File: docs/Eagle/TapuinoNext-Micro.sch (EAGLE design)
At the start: 10 parts

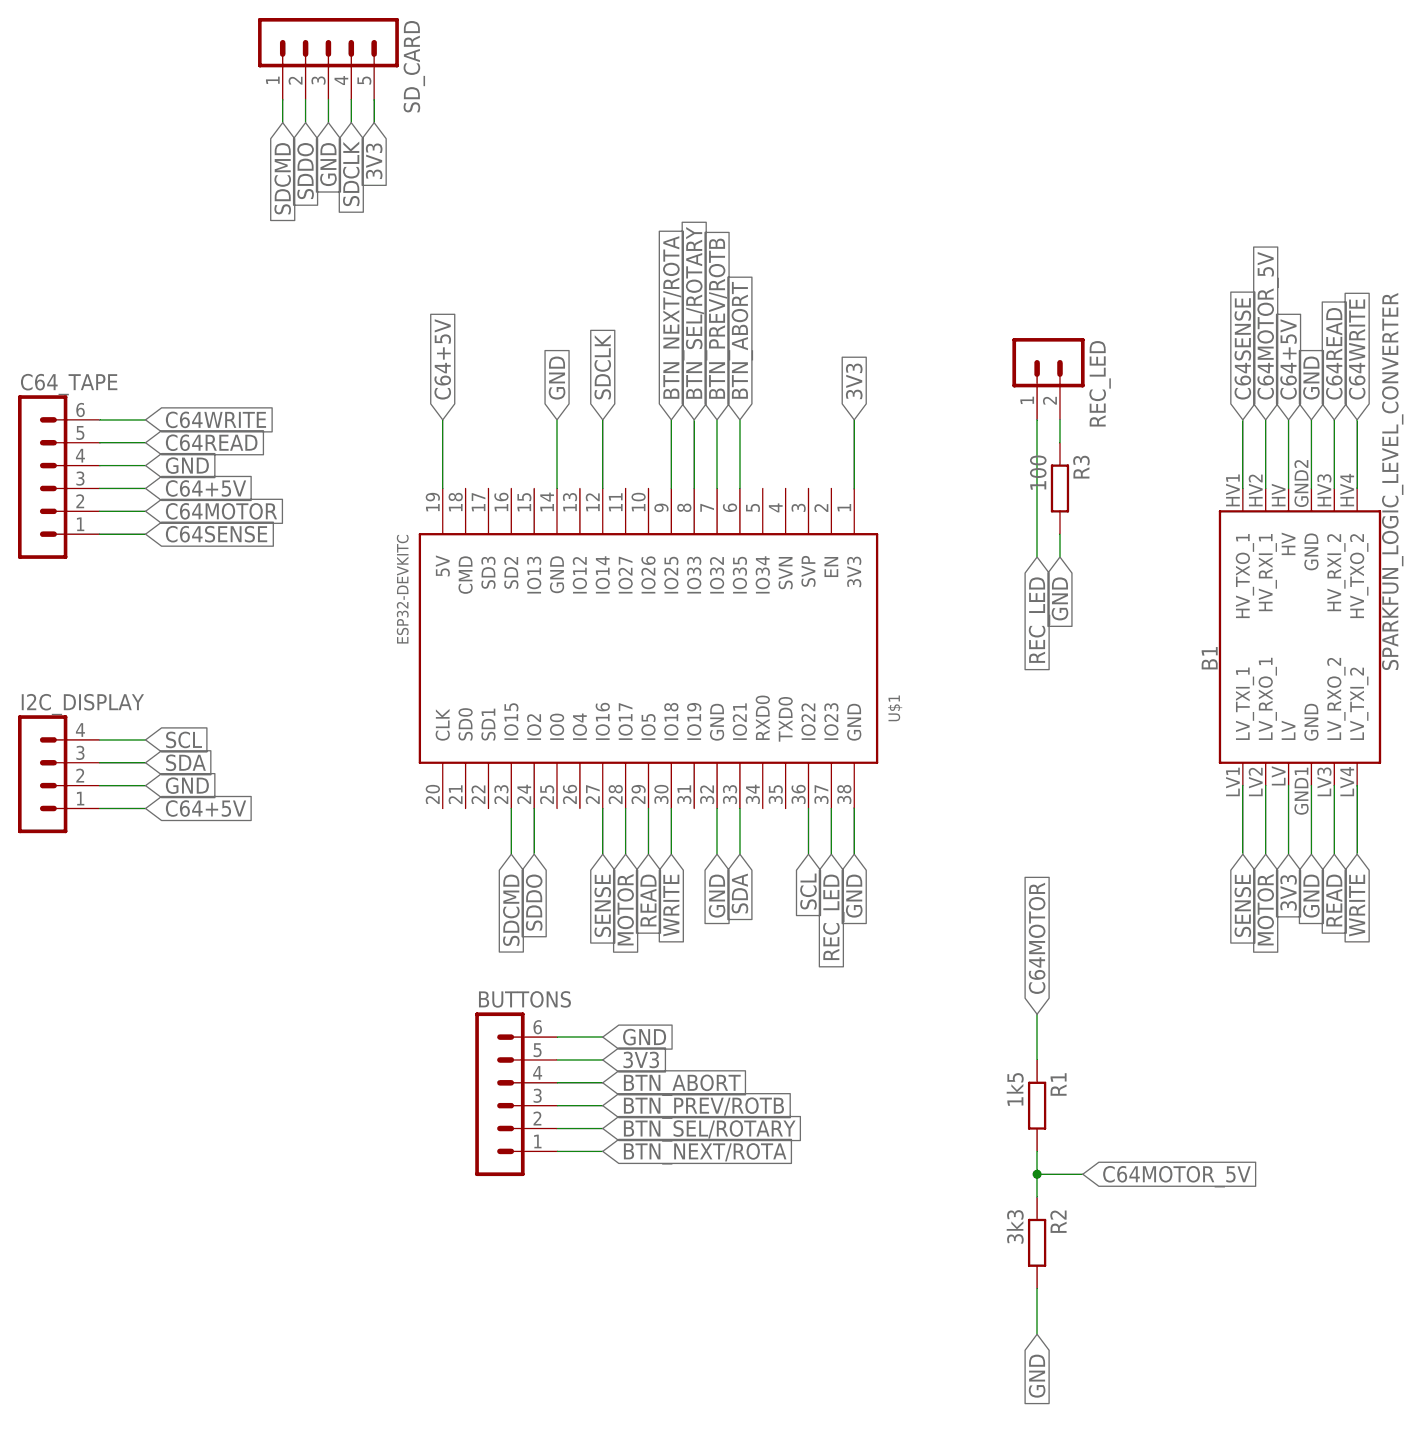
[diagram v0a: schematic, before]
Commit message: fixed definition for OLED1306 added the correct part for tthe ESP32 Devkit added a micro board for system builders (trying to keep this to the smallest footprint possible for custom builds) fixed the foot print on the reference board need to sort out constant changes to config.h to allow users changes outside of source control
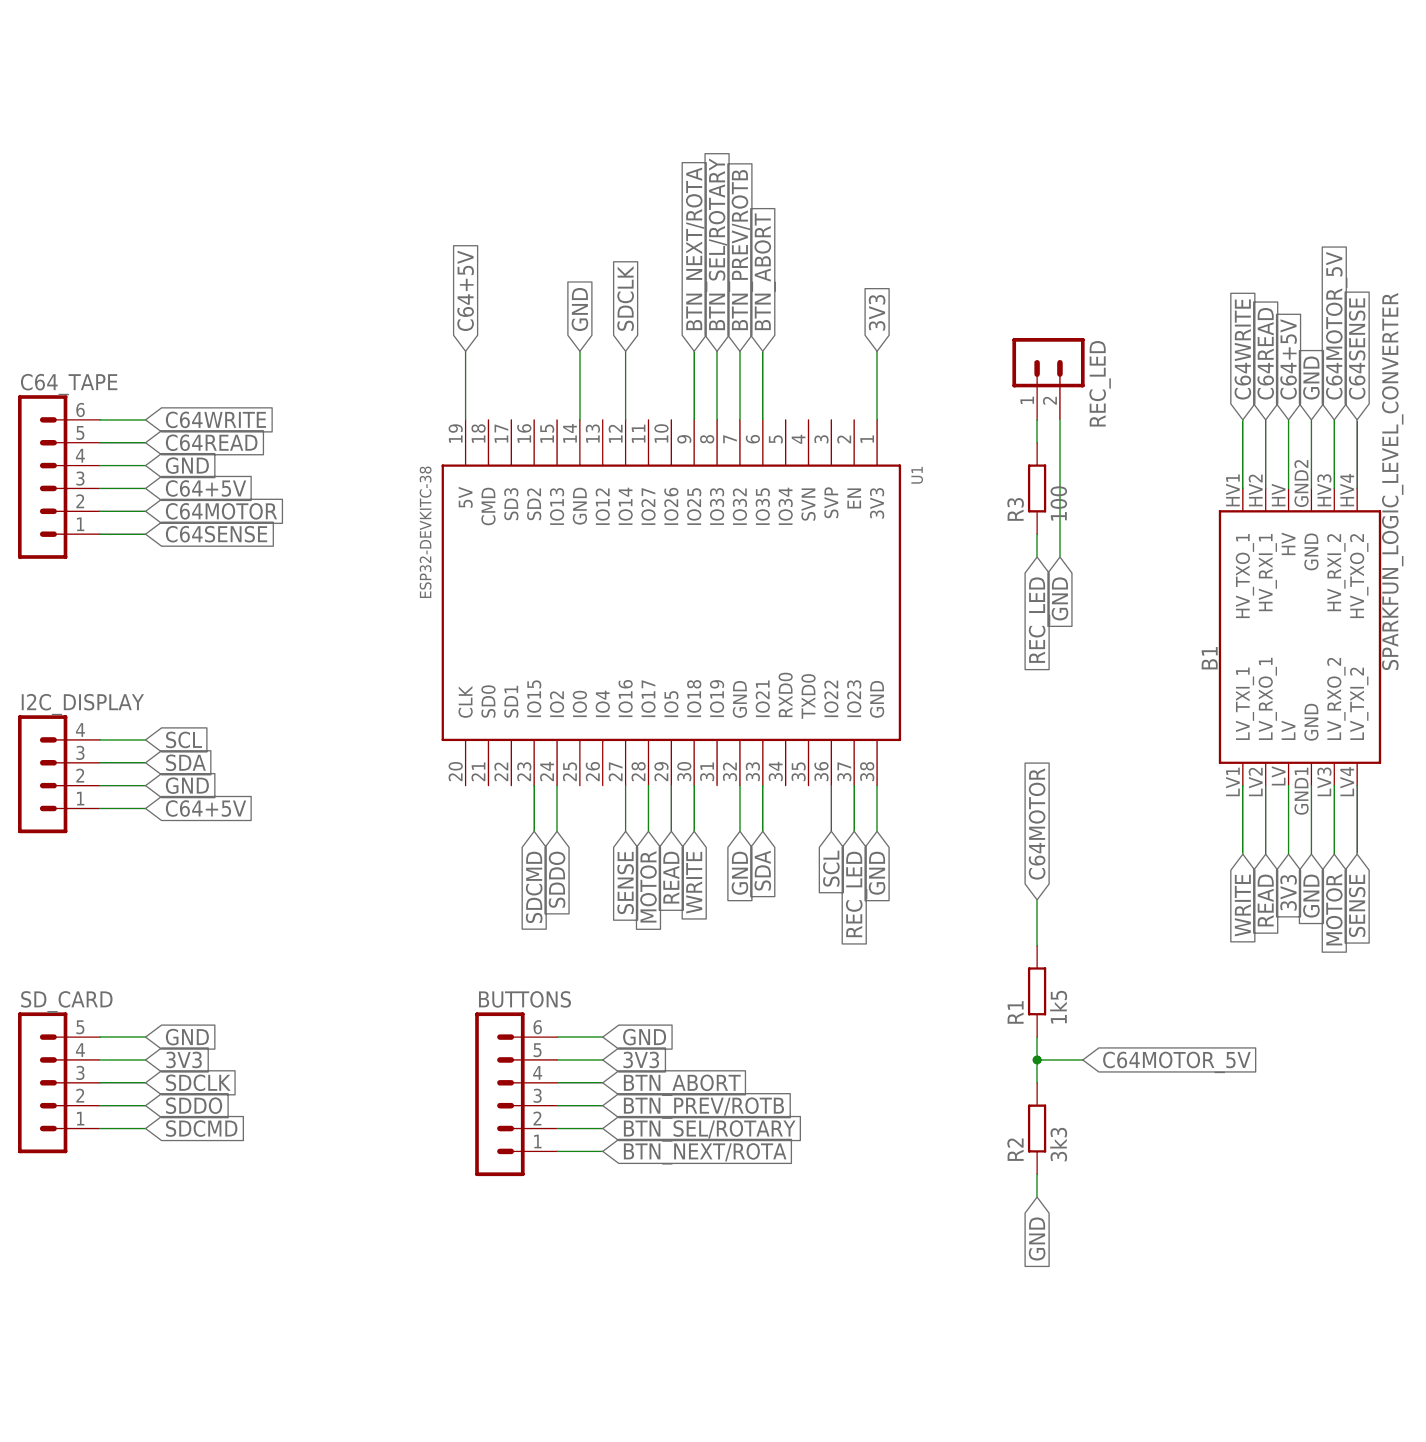
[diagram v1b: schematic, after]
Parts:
- removed U$1: ESP32DEVKITC, ESP32-DEVKITC:ESP32DEVKITC
- added U1: ESP32-DEVKITC-38, ESP32-DEVKITC-38PIN:ESP32-DEVKITC-38
- R1, R2, R3: device rcl:R-EU_0204/7 -> rcl:R-EU_M0805
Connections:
- removed net N$2: R3.1, REC_LED.2
- new net N$1: R3.2, REC_LED.1
- net 3V3: now also SD_CARD.4, U1.3V3; no longer SD_CARD.5, U$1.3V3
- net BTN_ABORT: now also U1.IO35; no longer U$1.IO35
- net BTN_NEXT/ROTA: now also U1.IO25; no longer U$1.IO25
- net BTN_PREV/ROTB: now also U1.IO32; no longer U$1.IO32
- net BTN_SEL/ROTARY: now also U1.IO33; no longer U$1.IO33
- net C64+5V: now also U1.5V; no longer U$1.5V
- net C64MOTOR: now also R1.2; no longer R1.1
- net C64MOTOR_5V: now also B1.HV_RXI_2, R1.1, R2.2; no longer B1.HV_RXI_1, R1.2, R2.1
- net C64READ: now also B1.HV_RXI_1; no longer B1.HV_RXI_2
- net C64SENSE: now also B1.HV_TXO_2; no longer B1.HV_TXO_1
- net C64WRITE: now also B1.HV_TXO_1; no longer B1.HV_TXO_2
- net GND: now also R2.1, REC_LED.2, SD_CARD.5, U1.GND@14, U1.GND@32, U1.GND@38; no longer R2.2, R3.2, SD_CARD.3, U$1.GND@14, U$1.GND@32, U$1.GND@38
- net MOTOR: now also B1.LV_RXO_2, U1.IO17; no longer B1.LV_RXO_1, U$1.IO17
- net READ: now also B1.LV_RXO_1, U1.IO5; no longer B1.LV_RXO_2, U$1.IO5
- net REC_LED: now also R3.1, U1.IO23; no longer REC_LED.1, U$1.IO23
- net SCL: now also U1.IO22; no longer U$1.IO22
- net SDA: now also U1.IO21; no longer U$1.IO21
- net SDCLK: now also SD_CARD.3, U1.IO14; no longer SD_CARD.4, U$1.IO14
- net SDCMD: now also U1.IO15; no longer U$1.IO15
- net SDDO: now also U1.IO2; no longer U$1.IO2
- net SENSE: now also B1.LV_TXI_2, U1.IO16; no longer B1.LV_TXI_1, U$1.IO16
- net WRITE: now also B1.LV_TXI_1, U1.IO18; no longer B1.LV_TXI_2, U$1.IO18
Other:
- moved on the sheet: R1, R2, R3, SD_CARD

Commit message: Changed rotary wiring back to original to match stripboard
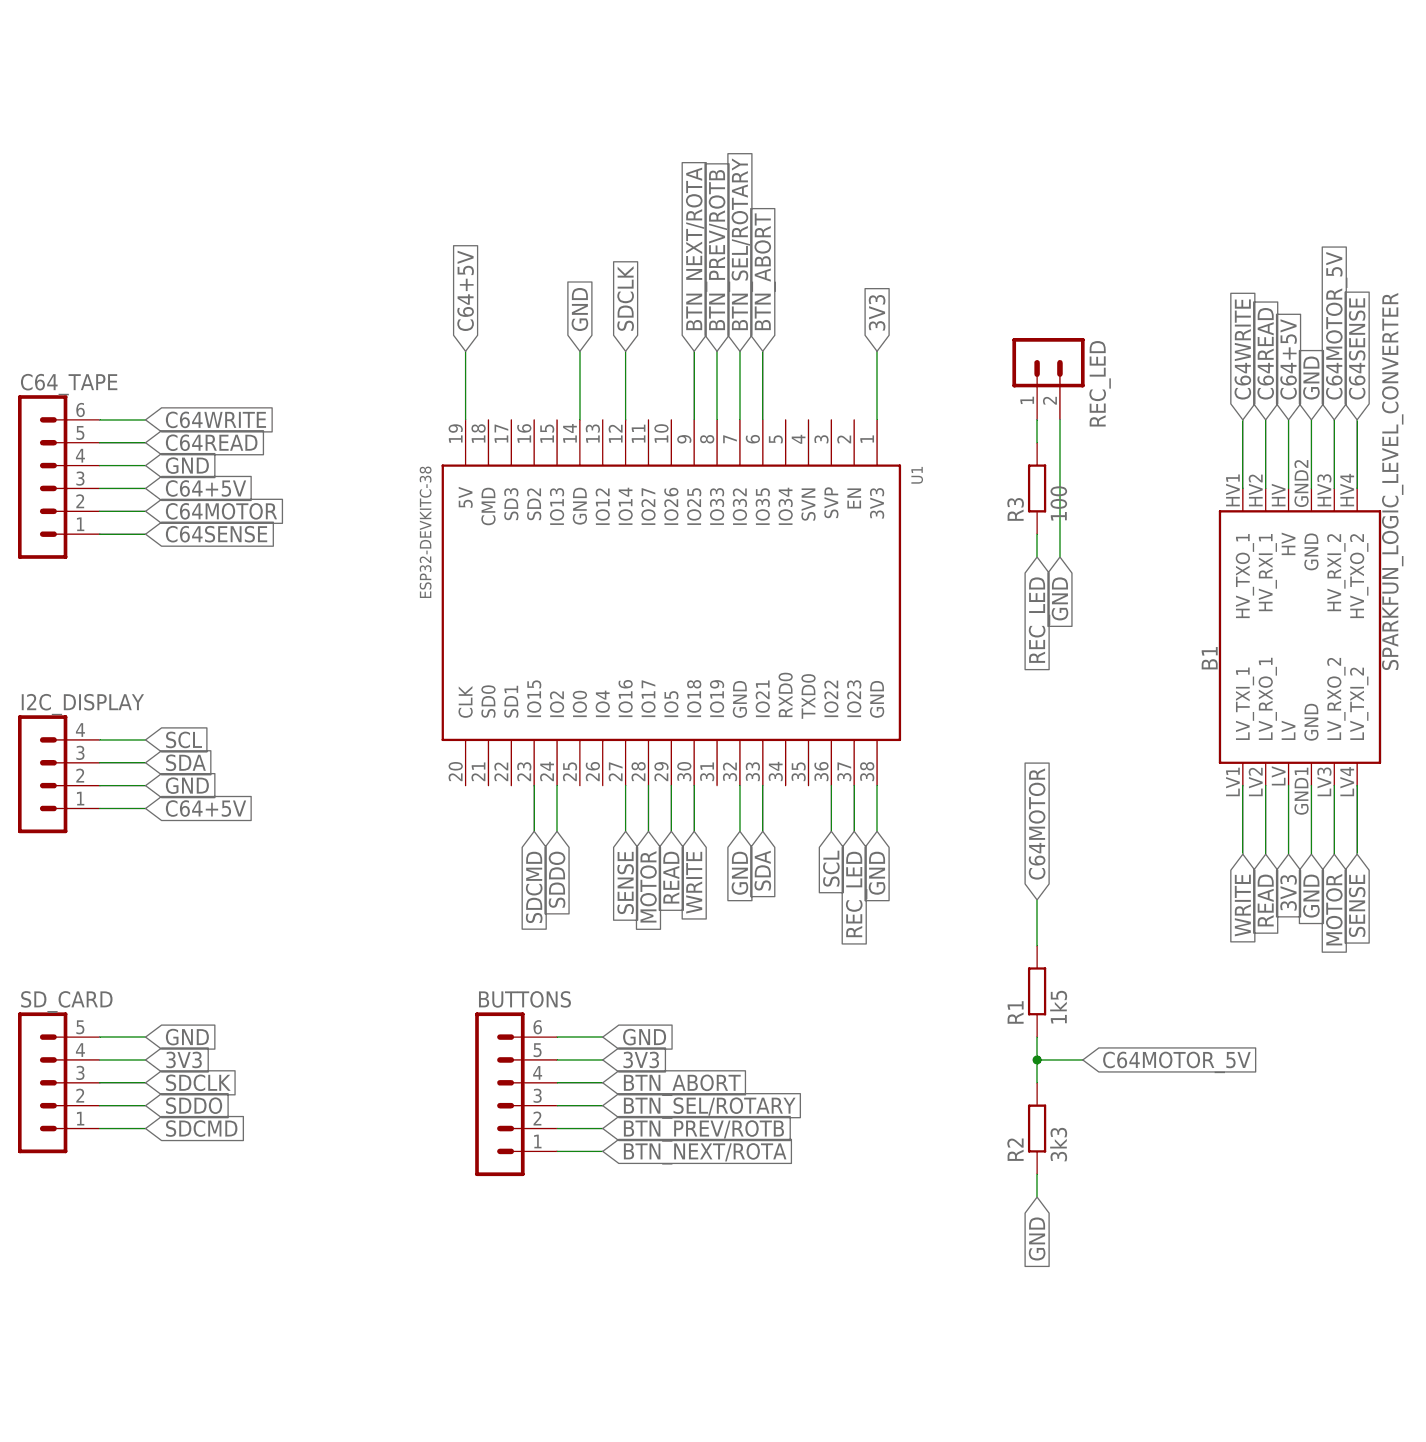
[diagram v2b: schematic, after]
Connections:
- net BTN_PREV/ROTB: now also BUTTONS.2, U1.IO33; no longer BUTTONS.3, U1.IO32
- net BTN_SEL/ROTARY: now also BUTTONS.3, U1.IO32; no longer BUTTONS.2, U1.IO33
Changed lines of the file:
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@@
 <net name="BTN_PREV/ROTB" class="0">
 <segment>
+<pinref part="U1" gate="G$1" pin="IO33"/>
+<wire x1="53.34" y1="68.58" x2="53.34" y2="76.2" width="0.1524" layer="91"/>
+<label x="53.34" y="76.2" size="1.778" layer="95" rot="R90" xref="yes"/>
+</segment>
+<segment>
+<pinref part="BUTTONS" gate="1" pin="2"/>
+<wire x1="35.56" y1="-10.16" x2="40.64" y2="-10.16" width="0.1524" layer="91"/>
+<label x="40.64" y="-10.16" size="1.778" layer="95" xref="yes"/>
+</segment>
+</net>
+<net name="BTN_SEL/ROTARY" class="0">
+<segment>
+<pinref part="U1" gate="G$1" pin="IO32"/>
 <wire x1="55.88" y1="68.58" x2="55.88" y2="76.2" width="0.1524" layer="91"/>
 <label x="55.88" y="76.2" size="1.778" layer="95" rot="R90" xref="yes"/>
-<pinref part="U1" gate="G$1" pin="IO32"/>
 </segment>
 <segment>
@@
 </segment>
 </net>
-<net name="BTN_SEL/ROTARY" class="0">
-<segment>
-<wire x1="53.34" y1="68.58" x2="53.34" y2="76.2" width="0.1524" layer="91"/>
-<label x="53.34" y="76.2" size="1.778" layer="95" rot="R90" xref="yes"/>
-<pinref part="U1" gate="G$1" pin="IO33"/>
-</segment>
-<segment>
-<pinref part="BUTTONS" gate="1" pin="2"/>
-<wire x1="35.56" y1="-10.16" x2="40.64" y2="-10.16" width="0.1524" layer="91"/>
-<label x="40.64" y="-10.16" size="1.778" layer="95" xref="yes"/>
-</segment>
-</net>

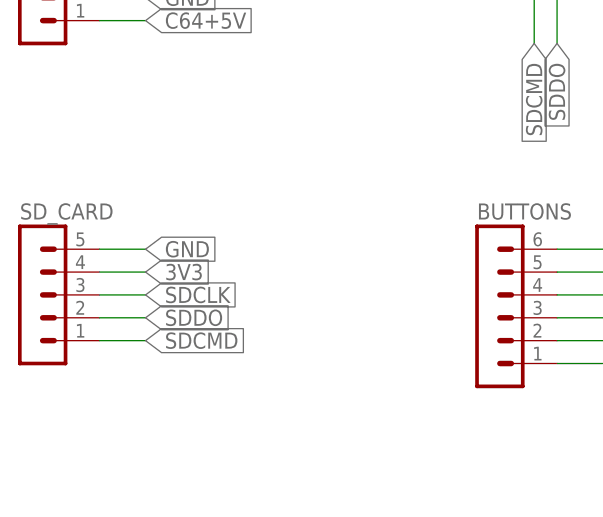
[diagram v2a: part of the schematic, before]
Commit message: Fixed pinout across all of the schematics, hopefully for the last time
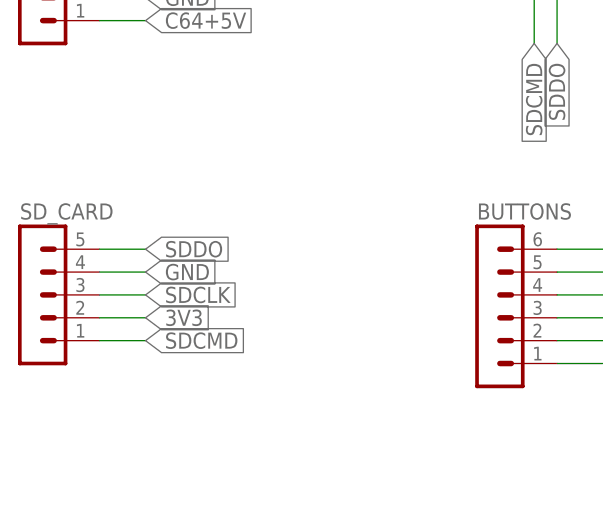
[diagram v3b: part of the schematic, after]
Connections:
- net 3V3: now also SD_CARD.2; no longer SD_CARD.4
- net GND: now also SD_CARD.4; no longer SD_CARD.5
- net SDDO: now also SD_CARD.5; no longer SD_CARD.2
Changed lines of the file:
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@@
-</segment>
-<segment>
-<pinref part="SD_CARD" gate="G$1" pin="5"/>
-<wire x1="-15.24" y1="0" x2="-10.16" y2="0" width="0.1524" layer="91"/>
-<label x="-10.16" y="0" size="1.778" layer="95" xref="yes"/>
 </segment>
 <segment>
@@
 <label x="91.44" y="53.34" size="1.778" layer="95" rot="R270" xref="yes"/>
 <pinref part="REC_LED" gate="G$1" pin="2"/>
+</segment>
+<segment>
+<pinref part="SD_CARD" gate="G$1" pin="4"/>
+<wire x1="-15.24" y1="-2.54" x2="-10.16" y2="-2.54" width="0.1524" layer="91"/>
+<label x="-10.16" y="-2.54" size="1.778" layer="95" xref="yes"/>
 </segment>
 </net>
@@
 </segment>
 <segment>
-<pinref part="SD_CARD" gate="G$1" pin="4"/>
-<wire x1="-15.24" y1="-2.54" x2="-10.16" y2="-2.54" width="0.1524" layer="91"/>
-<label x="-10.16" y="-2.54" size="1.778" layer="95" xref="yes"/>
+<pinref part="SD_CARD" gate="G$1" pin="2"/>
+<wire x1="-15.24" y1="-7.62" x2="-10.16" y2="-7.62" width="0.1524" layer="91"/>
+<label x="-10.16" y="-7.62" size="1.778" layer="95" xref="yes"/>
 </segment>
 </net>
@@
 </segment>
 <segment>
-<pinref part="SD_CARD" gate="G$1" pin="2"/>
-<wire x1="-15.24" y1="-7.62" x2="-10.16" y2="-7.62" width="0.1524" layer="91"/>
-<label x="-10.16" y="-7.62" size="1.778" layer="95" xref="yes"/>
+<pinref part="SD_CARD" gate="G$1" pin="5"/>
+<wire x1="-15.24" y1="0" x2="-10.16" y2="0" width="0.1524" layer="91"/>
+<label x="-10.16" y="0" size="1.778" layer="95" xref="yes"/>
 </segment>
 </net>
